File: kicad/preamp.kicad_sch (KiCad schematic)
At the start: 14 parts, among them Q1 MMBF5457, Q2 MMBF5457

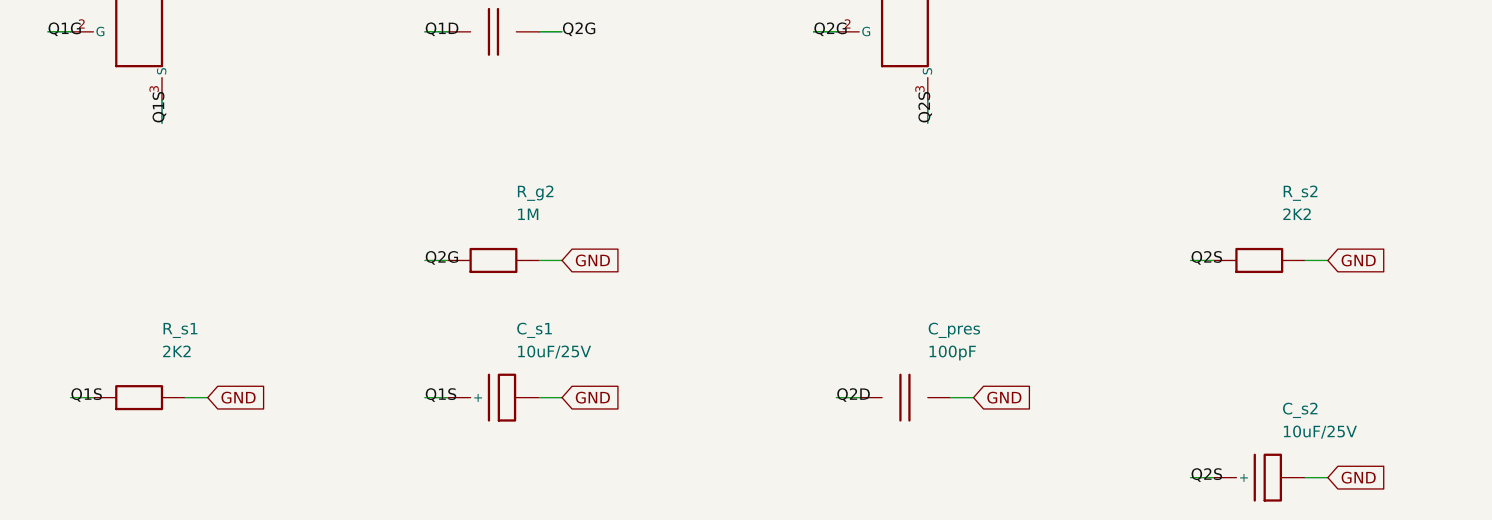
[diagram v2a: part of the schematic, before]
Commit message: Normalize BOM value strings; refresh stale top-level README
- gen_kicad NV(): normalize value strings for a tidy/consolidated BOM (2K2->2.2k,
  4K7->4.7k, drop the " film" descriptor that the footprint already conveys).
  Cosmetic only; ERC 0, demo DRC 0, SPICE exit 0, BOM regenerated.
- README rewritten to reflect the actual current state instead of the original
  reconstructed-docs snapshot: the generated + tool-verified KiCad/BOM/ngspice
  flow, the verified ~12 W power ceiling (not 18 W), the required mains fuse, the
  190x115 board + chassis-fit caveat, the active effects-chain/tone redesigns,
  and the provenance/honesty framing.

https://claude.ai/code/session_01PkrfUi9tvZfLvudJ7h23qD
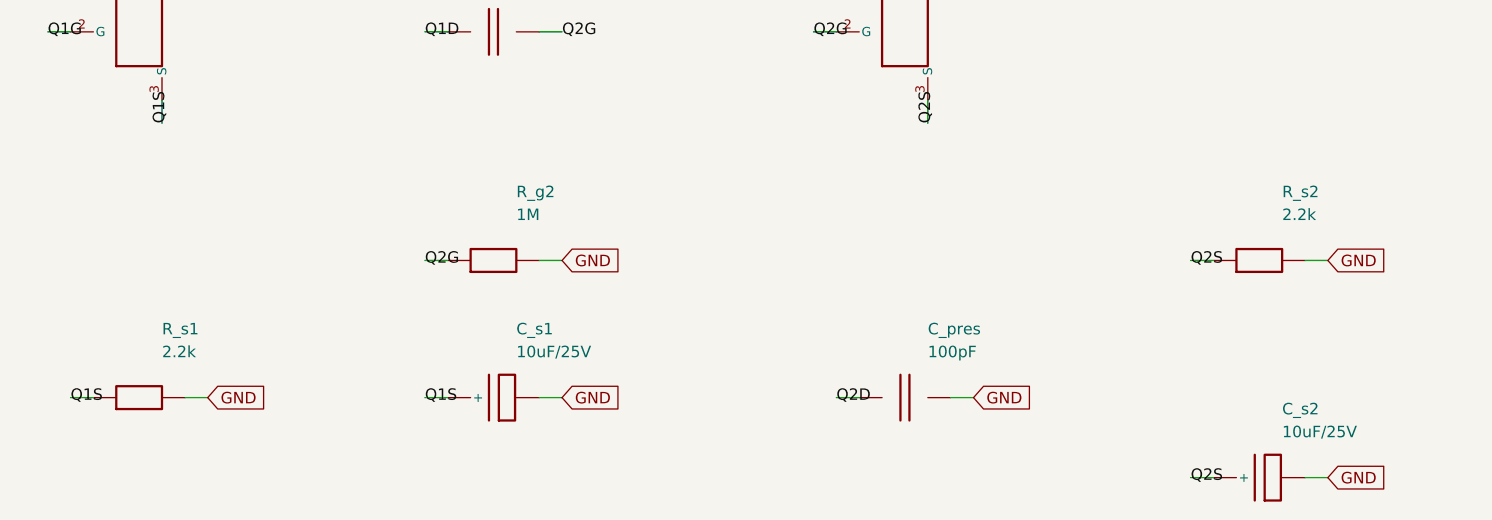
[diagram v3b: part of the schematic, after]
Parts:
- R_s1, R_s2: value 2K2 -> 2.2k
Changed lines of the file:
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@@
     (pin "1")
     (pin "2")
-    (instances (project "cambridge_reverb" (path "/18a02b70-cf92-46d8-9d8a-3d83a2b2b234" (reference "C_in_pre") (unit 1))))
+    (instances (project "cambridge_reverb" (path "/942ea049-022a-4522-9155-9a031f6385fe" (reference "C_in_pre") (unit 1))))
   )
   (wire (pts (xy 116.84 121.91999999999999) (xy 114.3 121.91999999999999)) (stroke (width 0) (type default)))
@@
     (pin "1")
     (pin "2")
-    (instances (project "cambridge_reverb" (path "/18a02b70-cf92-46d8-9d8a-3d83a2b2b234" (reference "R_g1") (unit 1))))
+    (instances (project "cambridge_reverb" (path "/942ea049-022a-4522-9155-9a031f6385fe" (reference "R_g1") (unit 1))))
   )
   (wire (pts (xy 116.84 152.4) (xy 114.3 152.4)) (stroke (width 0) (type default)))
@@
     (pin "1")
     (pin "3")
-    (instances (project "cambridge_reverb" (path "/18a02b70-cf92-46d8-9d8a-3d83a2b2b234" (reference "Q1") (unit 1))))
+    (instances (project "cambridge_reverb" (path "/942ea049-022a-4522-9155-9a031f6385fe" (reference "Q1") (unit 1))))
   )
   (wire (pts (xy 165.1 132.07999999999998) (xy 162.56 132.07999999999998)) (stroke (width 0) (type default)))
@@
     (pin "1")
     (pin "2")
-    (instances (project "cambridge_reverb" (path "/18a02b70-cf92-46d8-9d8a-3d83a2b2b234" (reference "R_d1") (unit 1))))
+    (instances (project "cambridge_reverb" (path "/942ea049-022a-4522-9155-9a031f6385fe" (reference "R_d1") (unit 1))))
   )
   (wire (pts (xy 167.64 101.6) (xy 165.1 101.6)) (stroke (width 0) (type default)))
@@
     (in_bom yes) (on_board yes) (dnp no)
     (property "Reference" "R_s1" (at 175.26 165.1 0) (effects (font (size 1.27 1.27)) (justify left)))
-    (property "Value" "2K2" (at 175.26 167.64 0) (effects (font (size 1.27 1.27)) (justify left)))
+    (property "Value" "2.2k" (at 175.26 167.64 0) (effects (font (size 1.27 1.27)) (justify left)))
     (property "Footprint" "Resistor_THT:R_Axial_DIN0207_L6.3mm_D2.5mm_P5.08mm_Vertical" (at 172.72 172.72 0) (effects (font (size 1.27 1.27)) hide))
     (pin "1")
     (pin "2")
-    (instances (project "cambridge_reverb" (path "/18a02b70-cf92-46d8-9d8a-3d83a2b2b234" (reference "R_s1") (unit 1))))
+    (instances (project "cambridge_reverb" (path "/942ea049-022a-4522-9155-9a031f6385fe" (reference "R_s1") (unit 1))))
   )
   (wire (pts (xy 167.64 172.72) (xy 165.1 172.72)) (stroke (width 0) (type default)))
@@
     (pin "1")
     (pin "2")
-    (instances (project "cambridge_reverb" (path "/18a02b70-cf92-46d8-9d8a-3d83a2b2b234" (reference "C_s1") (unit 1))))
+    (instances (project "cambridge_reverb" (path "/942ea049-022a-4522-9155-9a031f6385fe" (reference "C_s1") (unit 1))))
   )
   (wire (pts (xy 207.01 172.72) (xy 204.46999999999997 172.72)) (stroke (width 0) (type default)))
@@
     (pin "1")
     (pin "2")
-    (instances (project "cambridge_reverb" (path "/18a02b70-cf92-46d8-9d8a-3d83a2b2b234" (reference "C_cpl12") (unit 1))))
+    (instances (project "cambridge_reverb" (path "/942ea049-022a-4522-9155-9a031f6385fe" (reference "C_cpl12") (unit 1))))
   )
   (wire (pts (xy 207.01 132.07999999999998) (xy 204.46999999999997 132.07999999999998)) (stroke (width 0) (type default)))
@@
     (pin "1")
     (pin "2")
-    (instances (project "cambridge_reverb" (path "/18a02b70-cf92-46d8-9d8a-3d83a2b2b234" (reference "R_g2") (unit 1))))
+    (instances (project "cambridge_reverb" (path "/942ea049-022a-4522-9155-9a031f6385fe" (reference "R_g2") (unit 1))))
   )
   (wire (pts (xy 207.01 157.48) (xy 204.46999999999997 157.48)) (stroke (width 0) (type default)))
@@
     (pin "1")
     (pin "3")
-    (instances (project "cambridge_reverb" (path "/18a02b70-cf92-46d8-9d8a-3d83a2b2b234" (reference "Q2") (unit 1))))
+    (instances (project "cambridge_reverb" (path "/942ea049-022a-4522-9155-9a031f6385fe" (reference "Q2") (unit 1))))
   )
   (wire (pts (xy 250.19 132.07999999999998) (xy 247.64999999999998 132.07999999999998)) (stroke (width 0) (type default)))
@@
     (pin "1")
     (pin "2")
-    (instances (project "cambridge_reverb" (path "/18a02b70-cf92-46d8-9d8a-3d83a2b2b234" (reference "R_d2") (unit 1))))
+    (instances (project "cambridge_reverb" (path "/942ea049-022a-4522-9155-9a031f6385fe" (reference "R_d2") (unit 1))))
   )
   (wire (pts (xy 252.72999999999996 101.6) (xy 250.19 101.6)) (stroke (width 0) (type default)))
@@
     (pin "1")
     (pin "2")
-    (instances (project "cambridge_reverb" (path "/18a02b70-cf92-46d8-9d8a-3d83a2b2b234" (reference "C_pres") (unit 1))))
+    (instances (project "cambridge_reverb" (path "/942ea049-022a-4522-9155-9a031f6385fe" (reference "C_pres") (unit 1))))
   )
   (wire (pts (xy 252.72999999999996 172.72) (xy 250.19 172.72)) (stroke (width 0) (type default)))
@@
     (in_bom yes) (on_board yes) (dnp no)
     (property "Reference" "R_s2" (at 299.72 149.85999999999999 0) (effects (font (size 1.27 1.27)) (justify left)))
-    (property "Value" "2K2" (at 299.72 152.39999999999998 0) (effects (font (size 1.27 1.27)) (justify left)))
+    (property "Value" "2.2k" (at 299.72 152.39999999999998 0) (effects (font (size 1.27 1.27)) (justify left)))
     (property "Footprint" "Resistor_THT:R_Axial_DIN0207_L6.3mm_D2.5mm_P5.08mm_Vertical" (at 297.18 157.48 0) (effects (font (size 1.27 1.27)) hide))
     (pin "1")
     (pin "2")
-    (instances (project "cambridge_reverb" (path "/18a02b70-cf92-46d8-9d8a-3d83a2b2b234" (reference "R_s2") (unit 1))))
+    (instances (project "cambridge_reverb" (path "/942ea049-022a-4522-9155-9a031f6385fe" (reference "R_s2") (unit 1))))
   )
   (wire (pts (xy 292.09999999999997 157.48) (xy 289.56 157.48)) (stroke (width 0) (type default)))
@@
     (pin "1")
     (pin "2")
-    (instances (project "cambridge_reverb" (path "/18a02b70-cf92-46d8-9d8a-3d83a2b2b234" (reference "C_s2") (unit 1))))
+    (instances (project "cambridge_reverb" (path "/942ea049-022a-4522-9155-9a031f6385fe" (reference "C_s2") (unit 1))))
   )
   (wire (pts (xy 292.09999999999997 181.60999999999999) (xy 289.56 181.60999999999999)) (stroke (width 0) (type default)))
@@
     (pin "1")
     (pin "2")
-    (instances (project "cambridge_reverb" (path "/18a02b70-cf92-46d8-9d8a-3d83a2b2b234" (reference "C_treble") (unit 1))))
+    (instances (project "cambridge_reverb" (path "/942ea049-022a-4522-9155-9a031f6385fe" (reference "C_treble") (unit 1))))
   )
   (wire (pts (xy 292.09999999999997 116.84) (xy 289.56 116.84)) (stroke (width 0) (type default)))
